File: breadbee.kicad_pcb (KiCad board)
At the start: 4 copper layers, 32 x 30 mm, 83 parts, among them J1 HR961160C, J2 Conn_02x12_Odd_Even, J3 USB_B_Micro, J4 Conn_01x21, U1 msc313e, U2 spinor, U3 ea3036c, U4 ch340e, U5 tvsarray, Y1 Crystal_GND24

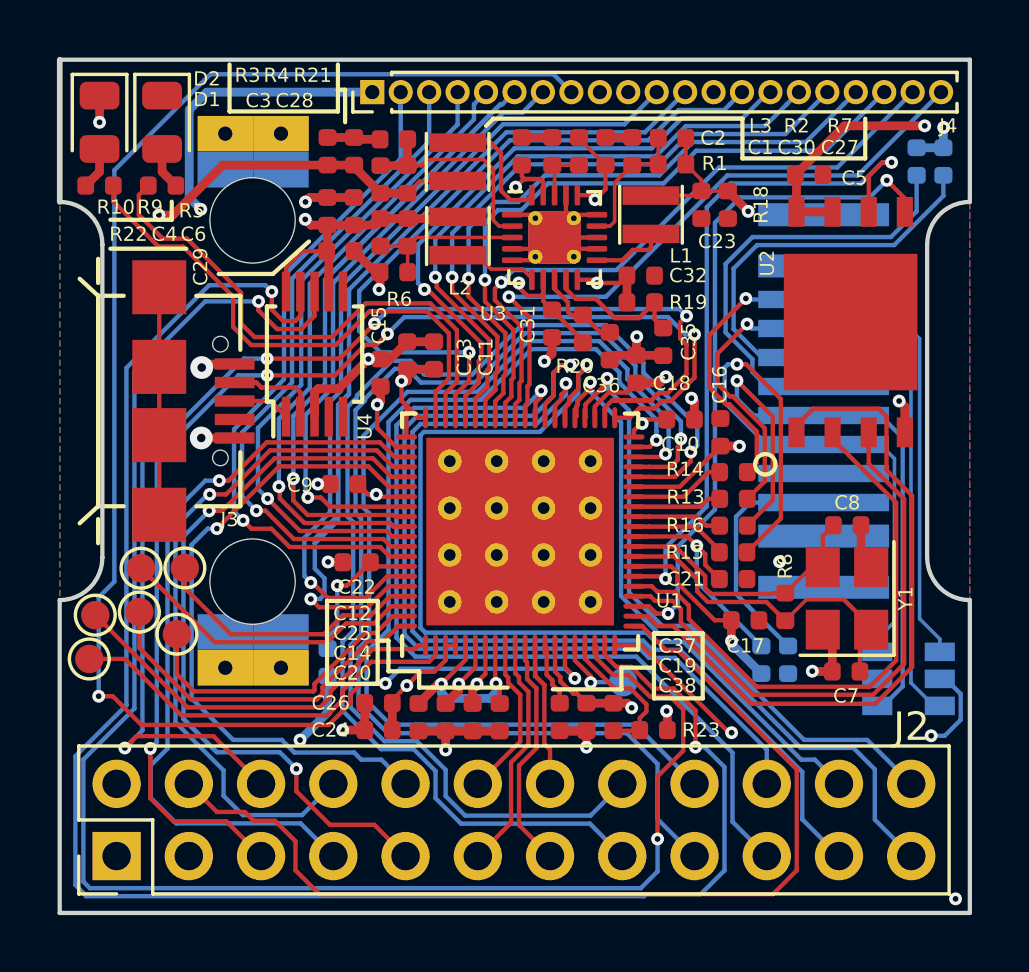
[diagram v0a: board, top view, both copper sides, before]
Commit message: pcb: remove redundant fragment of usb_dp
On a wire connecting the usb_dp to the header pin there was a redundant
fragment that was going on top of the actual wire connecting the whole
net. A small part of this wire had an offset making the wire ticker in
one place as well.

I noticed that by pure luck by manually going over the wire (after
pressing I). Unfortunately I don't know any method of automatically
finding such problems.

Note that in order to keep this change as small as possible I did not
run the refill of the bottom layer even though it could flow a little
more now that the thicker part of a wire is gone.
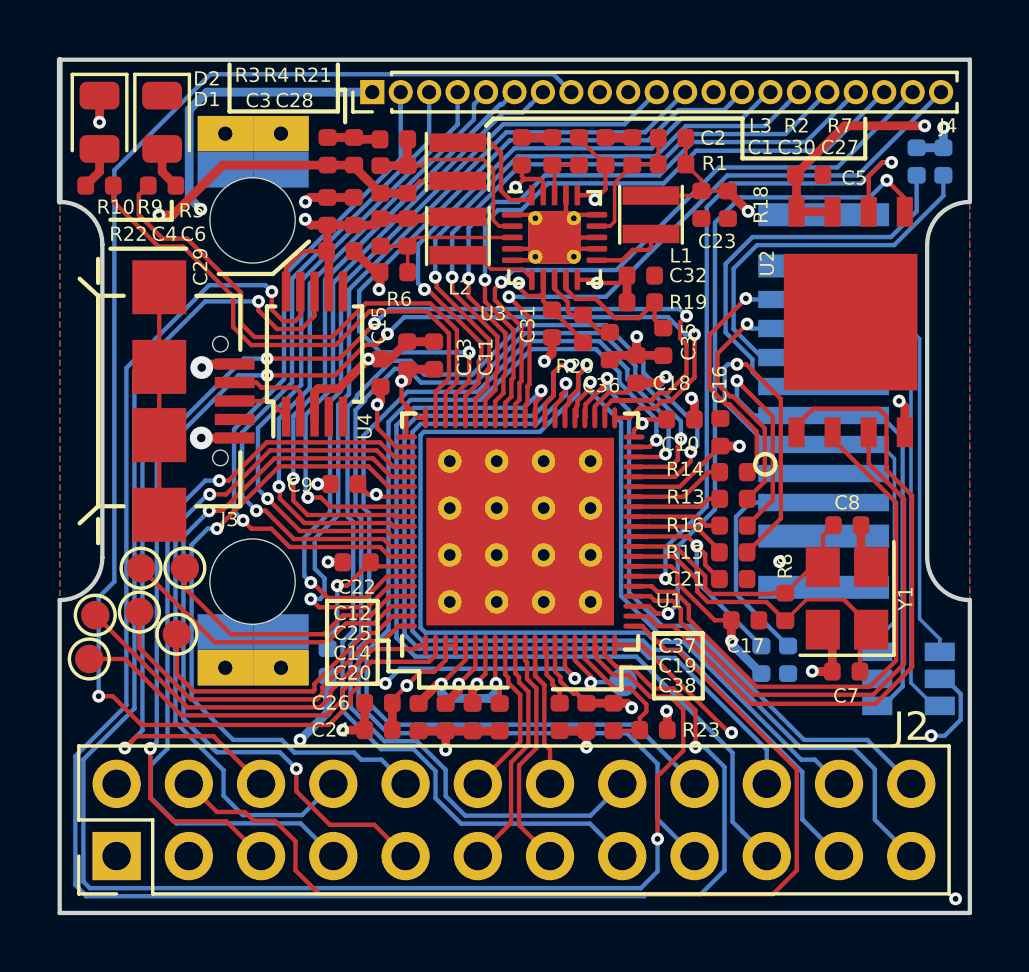
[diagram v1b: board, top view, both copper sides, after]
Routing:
- net /usb_dp: track 36.1 -> 30.4 mm
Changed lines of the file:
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@@
     (thickness 1.6)
     (drawings 48)
-    (tracks 1472)
+    (tracks 1469)
     (zones 0)
     (modules 83)
@@
   (segment (start 136.79 91.019998) (end 136.79 87.135865) (width 0.1545) (layer B.Cu) (net 60))
   (segment (start 136.79 87.135865) (end 137.172466 86.753399) (width 0.1545) (layer B.Cu) (net 60))
-  (segment (start 137.172466 86.753399) (end 136.786396 87.139469) (width 0.1545) (layer B.Cu) (net 60))
-  (segment (start 136.786396 87.139469) (end 136.786396 91.193604) (width 0.1545) (layer B.Cu) (net 60))
   (segment (start 135.969549 91.840451) (end 136.79 91.019998) (width 0.1545) (layer B.Cu) (net 60))
-  (segment (start 136.786396 91.193604) (end 135.969549 92.010451) (width 0.1545) (layer B.Cu) (net 60))
   (segment (start 137.172466 83.083186) (end 137.172466 86.753399) (width 0.1545) (layer B.Cu) (net 60))
   (segment (start 142.704141 77.551511) (end 137.172466 83.083186) (width 0.1545) (layer B.Cu) (net 60))
